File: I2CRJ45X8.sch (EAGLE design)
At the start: 51 parts, among them IC1 MCP23017SO, IC2 MCP23017SO, J1 M06-SOCKET, J2 M06-SOCKET, J3 M02X3-PIN, J4 M02X3-PIN

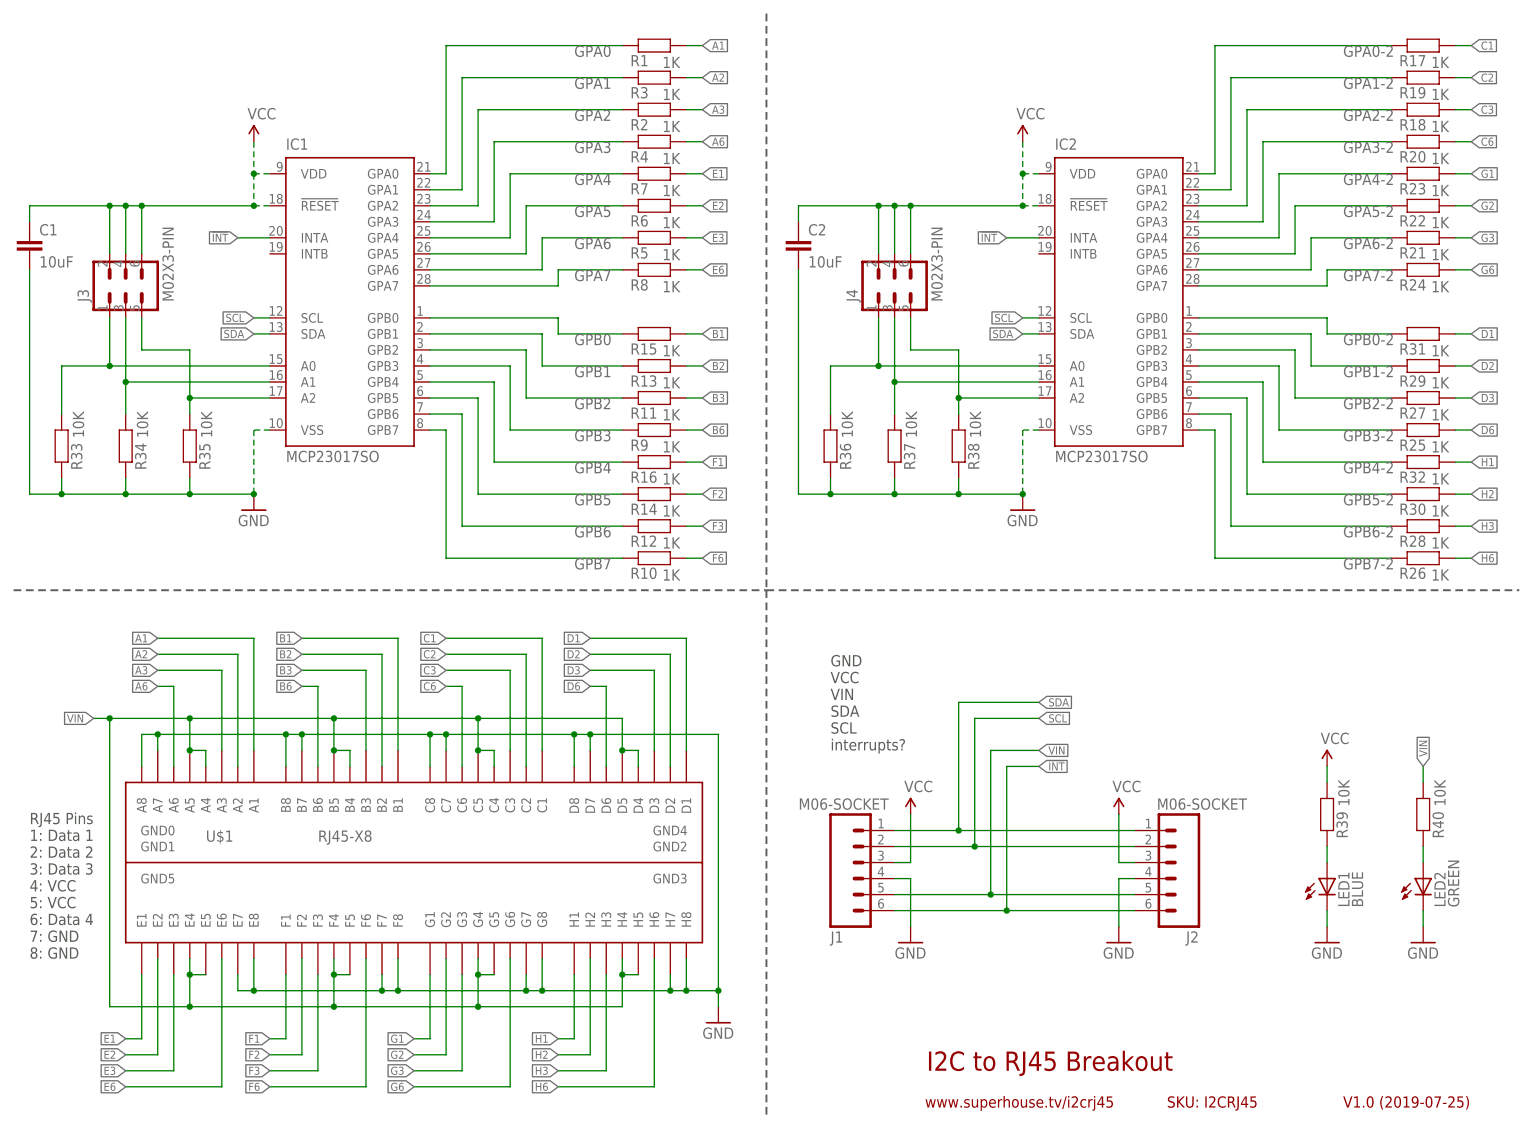
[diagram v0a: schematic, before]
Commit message: Board and schematic labelling
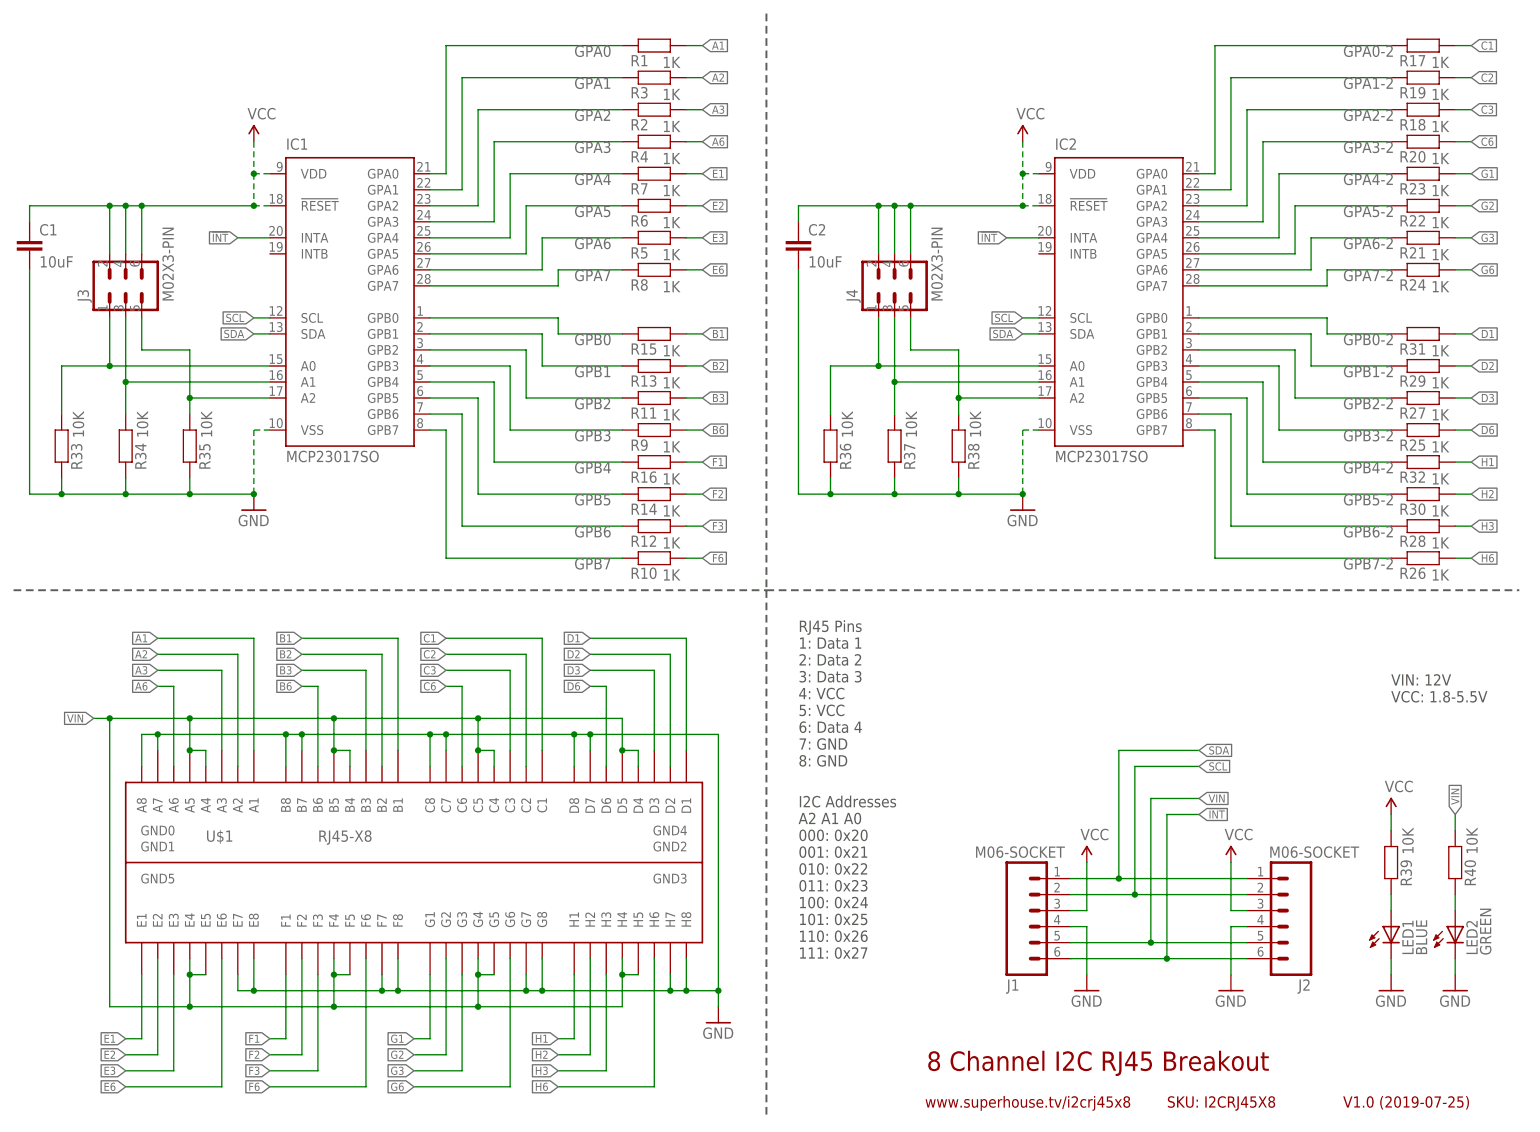
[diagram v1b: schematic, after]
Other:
- note added: "8 Channel I2C RJ45 Breakout"
- note added: "I2C Addresses A2 A1 A0 000: 0x20 001: 0x21 010: 0x22 011: 0x23 100: 0x24 101: 0x25 110: 0x26 111: 0x27"
- note added: "SKU: I2CRJ45X8"
- note added: "VIN: 12V VCC: 1.8-5.5V"
- note added: "www.superhouse.tv/i2crj45x8"
- note removed: "GND VCC VIN SDA SCL interrupts?"
- note removed: "I2C to RJ45 Breakout"
- note removed: "SKU: I2CRJ45"
- note removed: "www.superhouse.tv/i2crj45"
- moved on the sheet: J1, J2, LED1, LED2, R39, R40

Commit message: Part updates
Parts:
- renumbered U$1 to J5

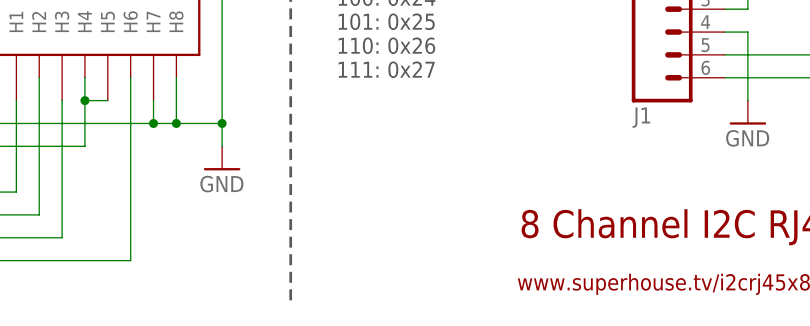
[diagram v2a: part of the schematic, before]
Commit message: Added fiducials
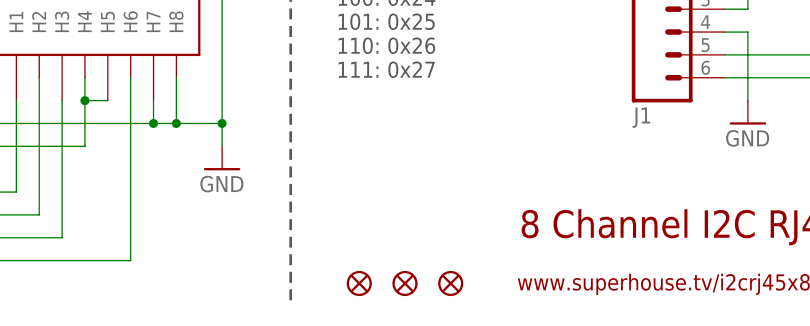
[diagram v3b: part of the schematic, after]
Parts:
- added FID1, FID2, FID3: FIDUCIAL1X2.5, freetronics:FIDUCIAL1X2.5
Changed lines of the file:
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@@
 <part name="GND6" library="SuperHouse-SupplySymbols" library_urn="urn:adsk.eagle:library:11790503" deviceset="GND" device=""/>
 <part name="GND7" library="SuperHouse-SupplySymbols" library_urn="urn:adsk.eagle:library:11790503" deviceset="GND" device=""/>
+<part name="FID1" library="freetronics" deviceset="FIDUCIAL" device="1X2.5"/>
+<part name="FID2" library="freetronics" deviceset="FIDUCIAL" device="1X2.5"/>
+<part name="FID3" library="freetronics" deviceset="FIDUCIAL" device="1X2.5"/>
 </parts>
 <sheets>
@@
 <attribute name="VALUE" x="231.14" y="22.86" size="1.778" layer="96"/>
 </instance>
+<instance part="FID1" gate="G$1" x="137.16" y="7.62" smashed="yes"/>
+<instance part="FID2" gate="G$1" x="142.24" y="7.62" smashed="yes"/>
+<instance part="FID3" gate="G$1" x="132.08" y="7.62" smashed="yes"/>
 </instances>
 <busses>

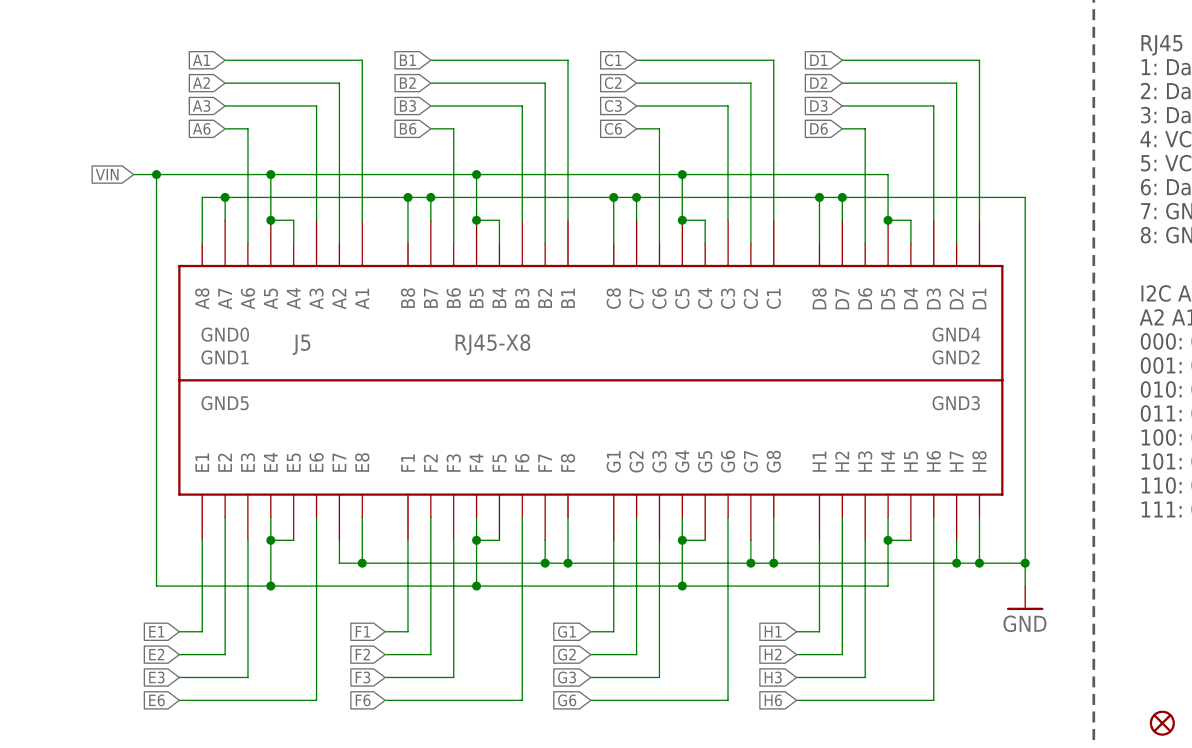
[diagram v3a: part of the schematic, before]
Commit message: Switched fiducials to SuperHouse library
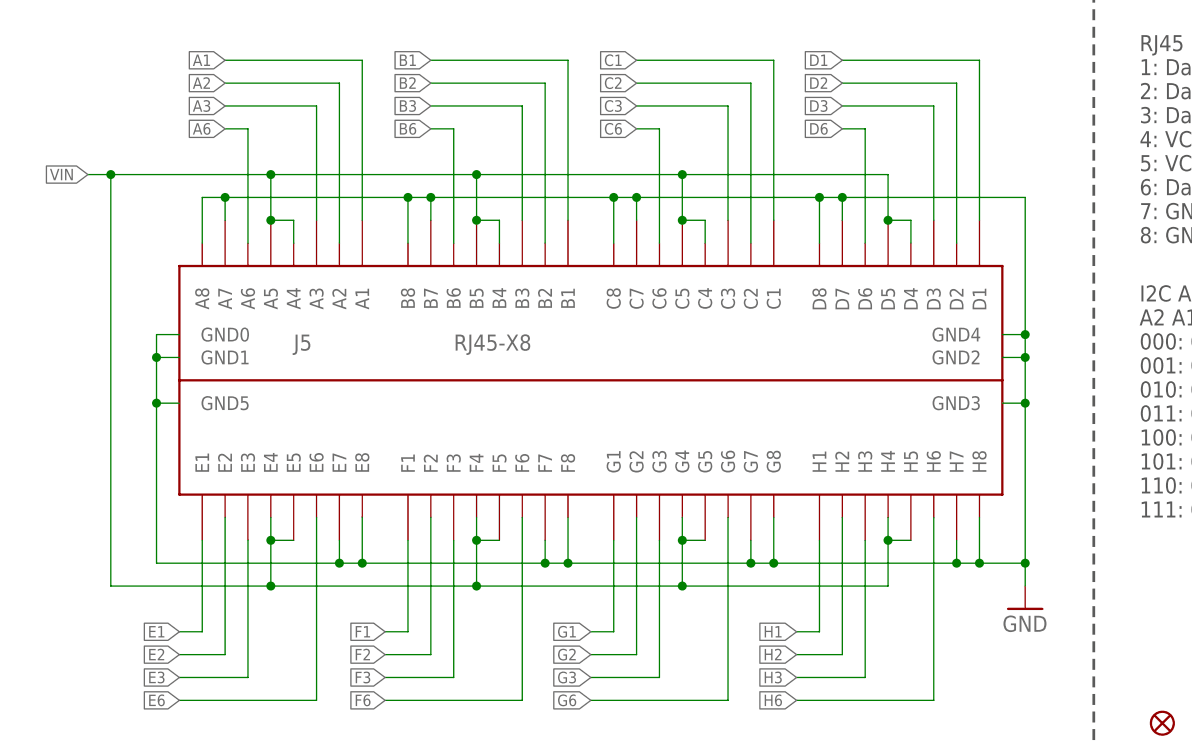
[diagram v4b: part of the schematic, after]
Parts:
- FID1, FID2, FID3: device freetronics:FIDUCIAL1X2.5 -> SuperHouse-Symbols:FIDUCIAL1X2.5
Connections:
- net GND: now also J5.GND0, J5.GND1, J5.GND2, J5.GND3, J5.GND4, J5.GND5
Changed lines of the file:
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@@
 <part name="GND6" library="SuperHouse-SupplySymbols" library_urn="urn:adsk.eagle:library:11790503" deviceset="GND" device=""/>
 <part name="GND7" library="SuperHouse-SupplySymbols" library_urn="urn:adsk.eagle:library:11790503" deviceset="GND" device=""/>
-<part name="FID1" library="freetronics" deviceset="FIDUCIAL" device="1X2.5"/>
-<part name="FID2" library="freetronics" deviceset="FIDUCIAL" device="1X2.5"/>
-<part name="FID3" library="freetronics" deviceset="FIDUCIAL" device="1X2.5"/>
+<part name="FID1" library="SuperHouse-Symbols" library_urn="urn:adsk.eagle:library:13228893" deviceset="FIDUCIAL" device="1X2.5" package3d_urn="urn:adsk.eagle:package:13228898/1"/>
+<part name="FID2" library="SuperHouse-Symbols" library_urn="urn:adsk.eagle:library:13228893" deviceset="FIDUCIAL" device="1X2.5" package3d_urn="urn:adsk.eagle:package:13228898/1"/>
+<part name="FID3" library="SuperHouse-Symbols" library_urn="urn:adsk.eagle:library:13228893" deviceset="FIDUCIAL" device="1X2.5" package3d_urn="urn:adsk.eagle:package:13228898/1"/>
 </parts>
 <sheets>
@@
 <wire x1="96.52" y1="66.04" x2="116.84" y2="66.04" width="0.1524" layer="91"/>
 <junction x="96.52" y="66.04"/>
-<wire x1="116.84" y1="66.04" x2="116.84" y2="25.4" width="0.1524" layer="91"/>
+<wire x1="116.84" y1="66.04" x2="116.84" y2="50.8" width="0.1524" layer="91"/>
 <junction x="116.84" y="25.4"/>
+<pinref part="J5" gate="G$1" pin="GND4"/>
+<wire x1="116.84" y1="50.8" x2="116.84" y2="48.26" width="0.1524" layer="91"/>
+<wire x1="116.84" y1="48.26" x2="116.84" y2="43.18" width="0.1524" layer="91"/>
+<wire x1="116.84" y1="43.18" x2="116.84" y2="25.4" width="0.1524" layer="91"/>
+<wire x1="114.3" y1="50.8" x2="116.84" y2="50.8" width="0.1524" layer="91"/>
+<junction x="116.84" y="50.8"/>
+<pinref part="J5" gate="G$1" pin="GND2"/>
+<wire x1="114.3" y1="48.26" x2="116.84" y2="48.26" width="0.1524" layer="91"/>
+<junction x="116.84" y="48.26"/>
+<pinref part="J5" gate="G$1" pin="GND3"/>
+<wire x1="114.3" y1="43.18" x2="116.84" y2="43.18" width="0.1524" layer="91"/>
+<junction x="116.84" y="43.18"/>
+<pinref part="J5" gate="G$1" pin="GND0"/>
+<wire x1="22.86" y1="50.8" x2="20.32" y2="50.8" width="0.1524" layer="91"/>
+<wire x1="20.32" y1="50.8" x2="20.32" y2="48.26" width="0.1524" layer="91"/>
+<pinref part="J5" gate="G$1" pin="GND1"/>
+<wire x1="20.32" y1="48.26" x2="20.32" y2="43.18" width="0.1524" layer="91"/>
+<wire x1="20.32" y1="43.18" x2="20.32" y2="25.4" width="0.1524" layer="91"/>
+<wire x1="22.86" y1="48.26" x2="20.32" y2="48.26" width="0.1524" layer="91"/>
+<junction x="20.32" y="48.26"/>
+<pinref part="J5" gate="G$1" pin="GND5"/>
+<wire x1="22.86" y1="43.18" x2="20.32" y2="43.18" width="0.1524" layer="91"/>
+<junction x="20.32" y="43.18"/>
+<wire x1="20.32" y1="25.4" x2="40.64" y2="25.4" width="0.1524" layer="91"/>
+<junction x="40.64" y="25.4"/>
 </segment>
 <segment>
@@
 <wire x1="78.74" y1="22.86" x2="55.88" y2="22.86" width="0.1524" layer="91"/>
 <wire x1="55.88" y1="22.86" x2="33.02" y2="22.86" width="0.1524" layer="91"/>
-<wire x1="33.02" y1="22.86" x2="20.32" y2="22.86" width="0.1524" layer="91"/>
+<wire x1="33.02" y1="22.86" x2="15.24" y2="22.86" width="0.1524" layer="91"/>
 <wire x1="33.02" y1="27.94" x2="33.02" y2="22.86" width="0.1524" layer="91"/>
 <junction x="33.02" y="27.94"/>
@@
 <pinref part="J5" gate="G$1" pin="D5"/>
 <wire x1="104.14" y1="63.5" x2="101.6" y2="63.5" width="0.1524" layer="91"/>
-<wire x1="17.78" y1="68.58" x2="20.32" y2="68.58" width="0.1524" layer="91"/>
-<wire x1="20.32" y1="68.58" x2="33.02" y2="68.58" width="0.1524" layer="91"/>
+<wire x1="12.7" y1="68.58" x2="15.24" y2="68.58" width="0.1524" layer="91"/>
+<wire x1="15.24" y1="68.58" x2="33.02" y2="68.58" width="0.1524" layer="91"/>
 <wire x1="33.02" y1="68.58" x2="55.88" y2="68.58" width="0.1524" layer="91"/>
 <wire x1="55.88" y1="68.58" x2="78.74" y2="68.58" width="0.1524" layer="91"/>
@@
 <junction x="33.02" y="63.5"/>
 <junction x="33.02" y="68.58"/>
-<label x="17.78" y="68.58" size="1.27" layer="95" rot="R180" xref="yes"/>
-<wire x1="20.32" y1="22.86" x2="20.32" y2="68.58" width="0.1524" layer="91"/>
-<junction x="20.32" y="68.58"/>
+<label x="12.7" y="68.58" size="1.27" layer="95" rot="R180" xref="yes"/>
+<wire x1="15.24" y1="22.86" x2="15.24" y2="68.58" width="0.1524" layer="91"/>
+<junction x="15.24" y="68.58"/>
 </segment>
 <segment>
@@
 </sheet>
 </sheets>
+<errors>
+</errors>
 </schematic>
 </drawing>
